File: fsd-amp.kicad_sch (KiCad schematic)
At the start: 13 parts, among them J1001 Screw_Terminal_01x06, J1004 AudioJack2_Ground_Switch, Q1001 FZT 653 ZET, Q1002 FZT 653 ZET, Q1003 FZT 753 ZET

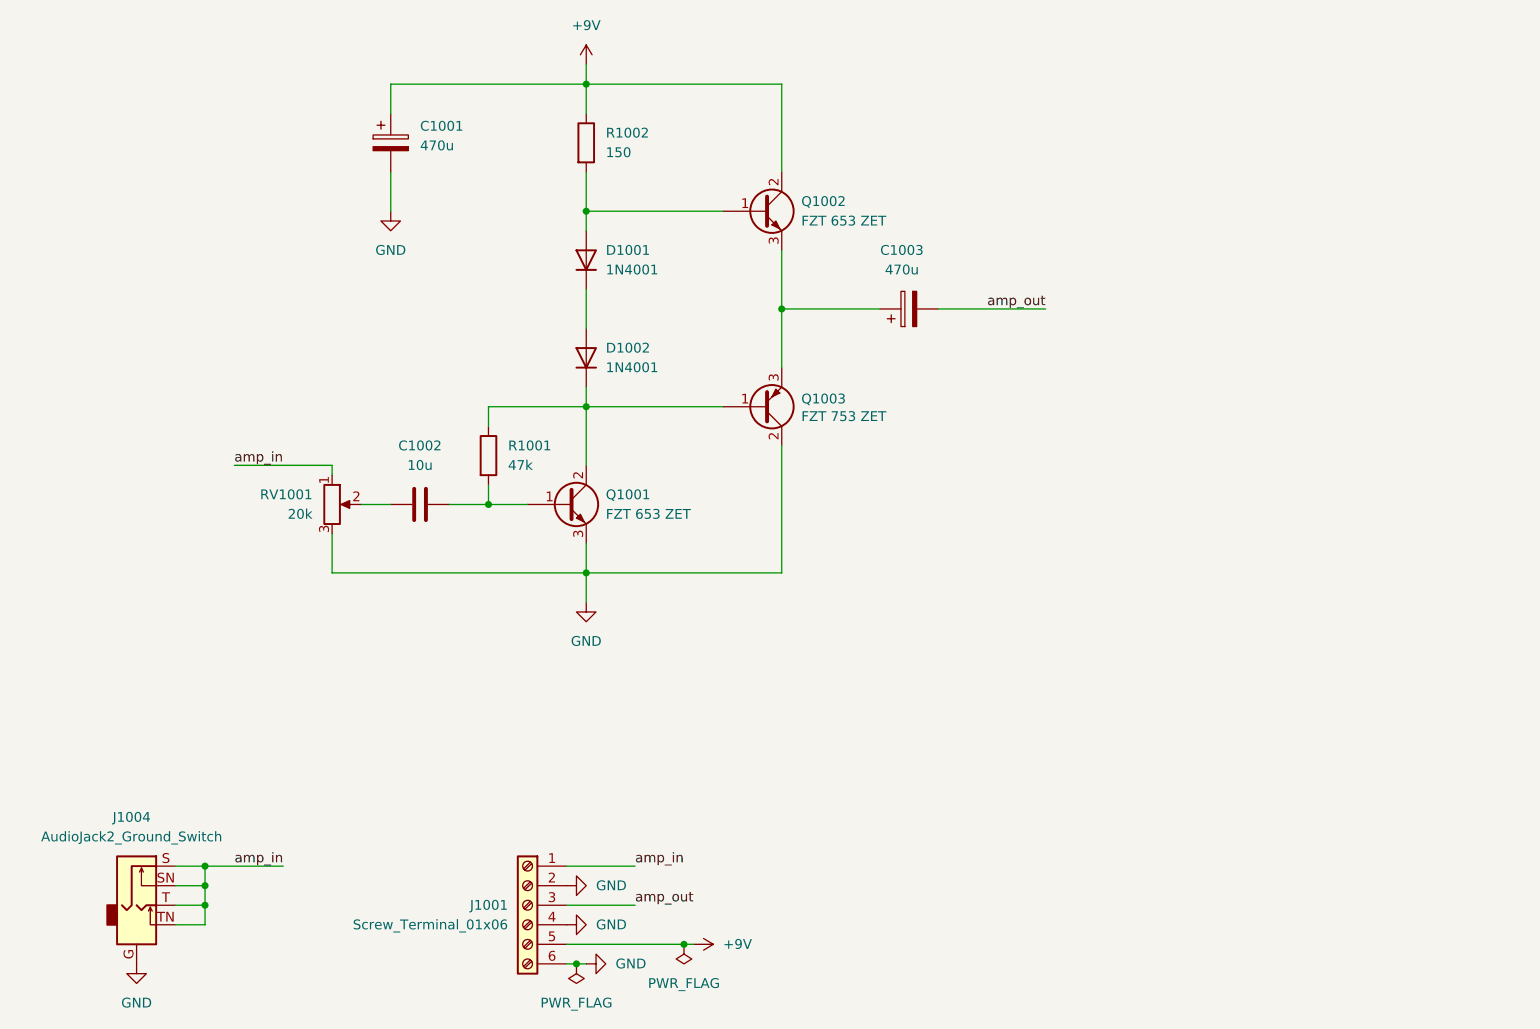
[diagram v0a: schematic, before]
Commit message: add backup THT transistor footprint
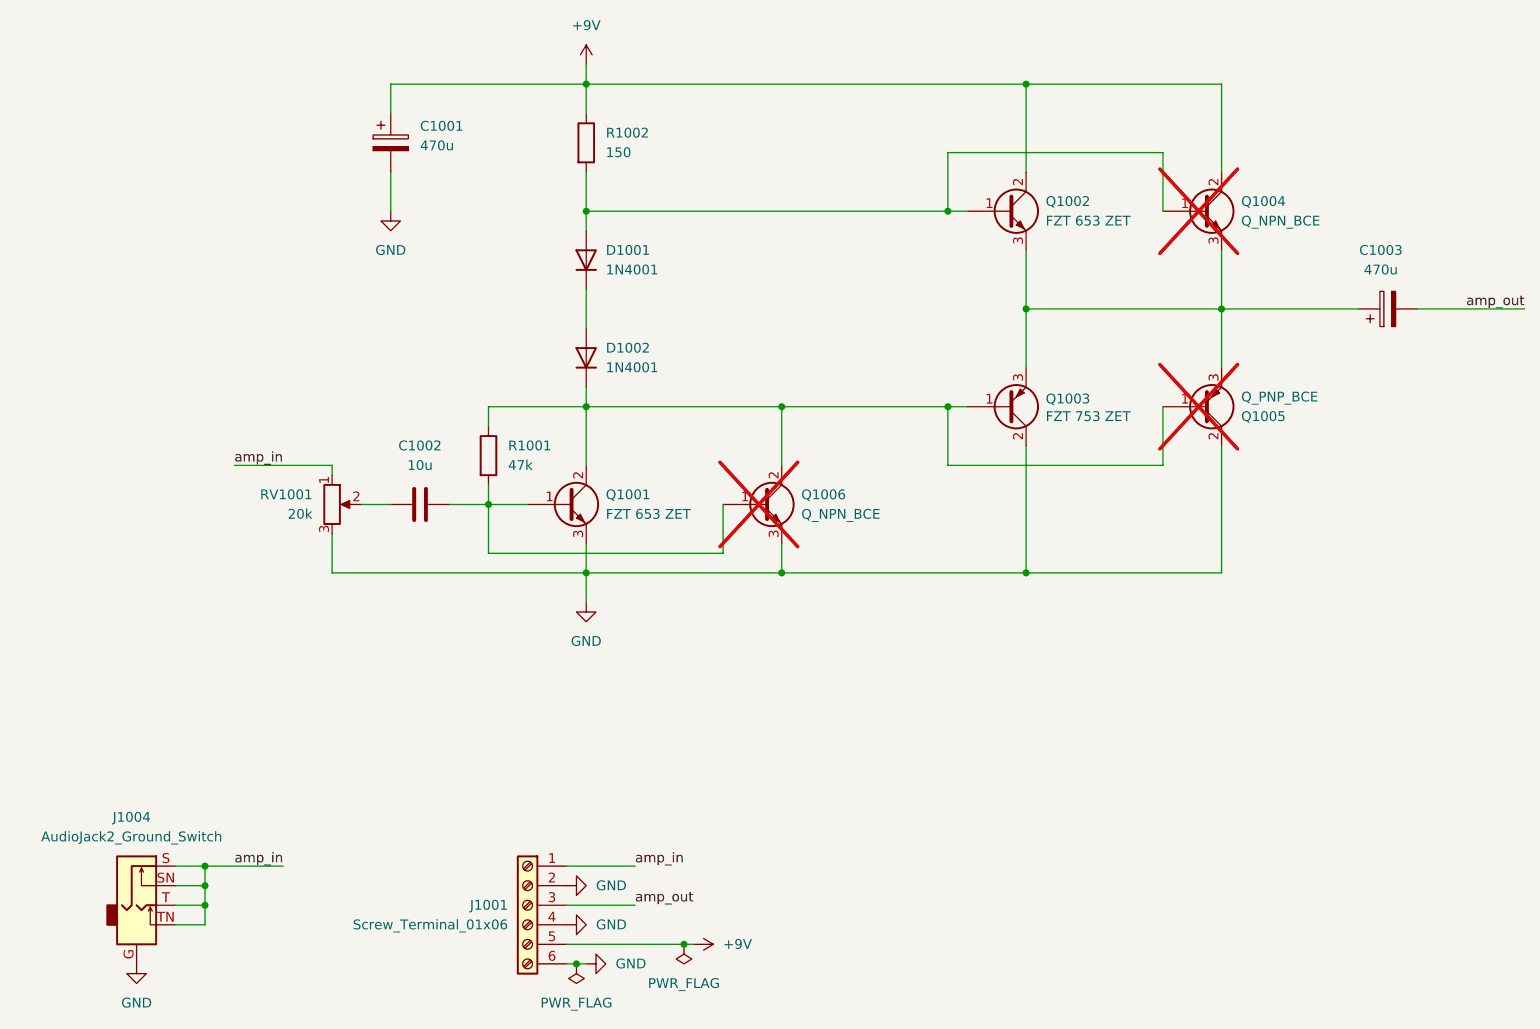
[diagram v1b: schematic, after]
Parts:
- added Q1004, Q1006: Q_NPN_BCE, fp:TO-92_Inline_Wide_NOcourtyard, symbol sym:Q_NPN_BCE
- added Q1005: Q_PNP_BCE, fp:TO-92_Inline_Wide_NOcourtyard, symbol sym:Q_PNP_BCE
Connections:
- net +9V: now also Q1004.2 (C)
- net GND: now also Q1005.2 (C), Q1006.3 (E)
- net at D1002.1 (K), Q1001.2 (C), Q1003.1 (B)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: now also Q1005.1 (B), Q1006.2 (C)
- net at C1003.1, Q1002.3 (E), Q1003.3 (E): now also Q1004.3 (E), Q1005.3 (E)
- net at D1001.2 (A), Q1002.1 (B), R1002.2: now also Q1004.1 (B)
- net at C1002.2, Q1001.1 (B), R1001.2: now also Q1006.1 (B)
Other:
- moved on the sheet: C1003, Q1002, Q1003

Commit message: fix excess quiescent current
- bias voltage is to high resulting in excess current flow of approx 1A in the complementary emitter follower
- replace D1002 from diode to wire bridge to reduce the bias voltage
´
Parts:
- D1002: value 1N4001 -> Wire Bridge; VLNK https://www.reichelt.de/gleichrichterdiode-50-v-1-a-do-41-1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 -> (none); VPN 1N 4001 -> Wire Bridge
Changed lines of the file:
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@@
 	(title_block
 		(title "FSD-Amp")
-		(date "2024-05-24")
-		(rev "1.0.0")
+		(date "2024-06-09")
+		(rev "1.0.1")
 	)
 	(junction
@@
 			)
 		)
-		(property "Value" "1N4001"
+		(property "Value" "Wire Bridge"
 			(at 149.86 101.5999 90)
 			(effects
@@
 			)
 		)
-		(property "Datasheet" "https://cdn-reichelt.de/documents/datenblatt/A400/1N4001-1N4007_LUNSURE.pdf"
+		(property "Datasheet" ""
 			(at 147.32 100.33 0)
 			(effects
@@
 			)
 		)
-		(property "VLNK" "https://www.reichelt.de/gleichrichterdiode-50-v-1-a-do-41-1n-4001-p1723.html?&trstct=pos_0&nbc=1"
+		(property "VLNK" ""
 			(at 147.32 100.33 0)
 			(effects
@@
 			)
 		)
-		(property "VPN" "1N 4001"
+		(property "VPN" "Wire Bridge"
 			(at 147.32 100.33 0)
 			(effects
